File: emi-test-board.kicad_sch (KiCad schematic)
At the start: 1 part, among them U1 XL1509-3.3

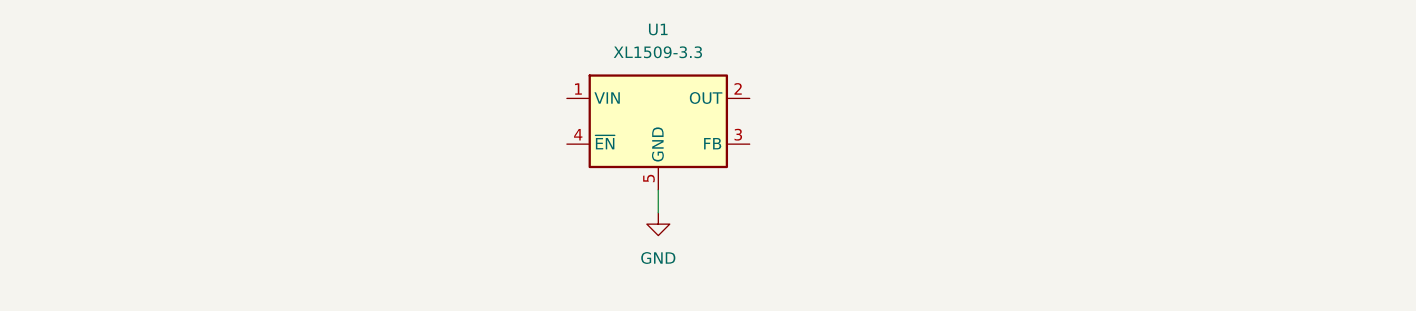
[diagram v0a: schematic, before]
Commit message: feat: XL1509-3.3 buck-converter schematic
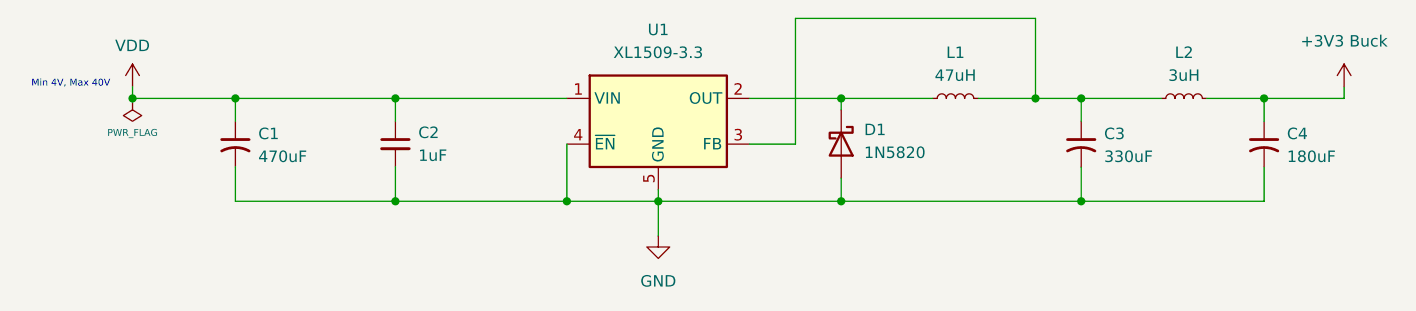
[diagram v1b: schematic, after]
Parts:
- added C1: 470uF, symbol Device:C_Small_US
- added C2: 1uF, symbol Device:C_Small
- added C3: 330uF, symbol Device:C_Small_US
- added C4: 180uF, symbol Device:C_Small_US
- added D1: 1N5820, symbol Device:D_Schottky
- added L1: 47uH, symbol Device:L_Small
- added L2: 3uH, symbol Device:L_Small
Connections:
- net GND: now also U1.4 (~{EN}), C1.2, C2.2, C3.2, C4.2, D1.2 (A)
- net VDD: now reaches U1.1 (VIN)
- net VDD: now also C1.1, C2.1
- net at U1.2 (OUT): now also D1.1 (K), L1.1
- net at U1.3 (FB): now also C3.1, L1.2, L2.1
- new net +3V3 Buck: C4.1, L2.2
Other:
- note added: "Min 4V, Max 40V"

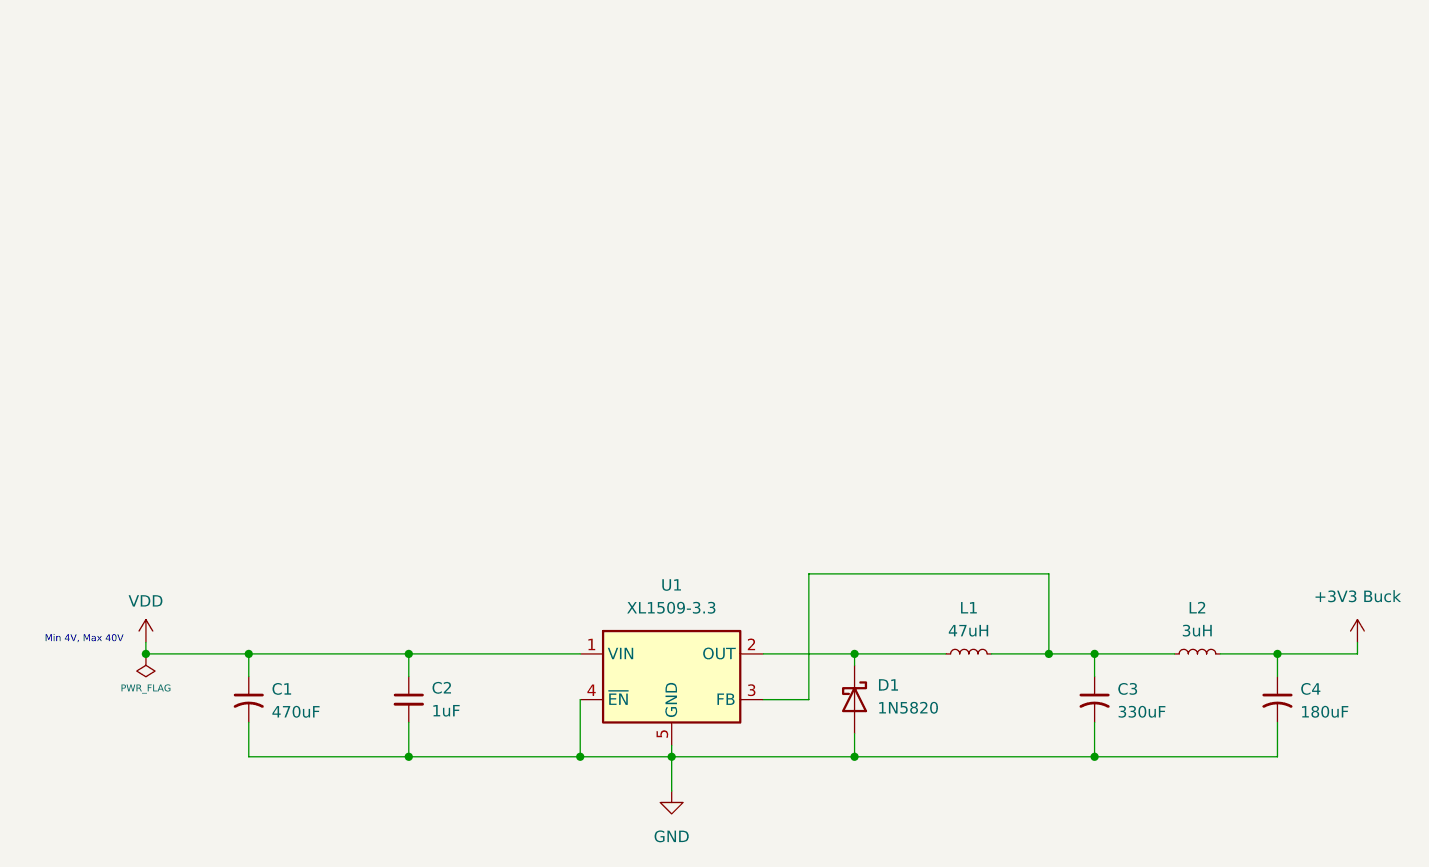
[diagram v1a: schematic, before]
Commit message: feat: component selection
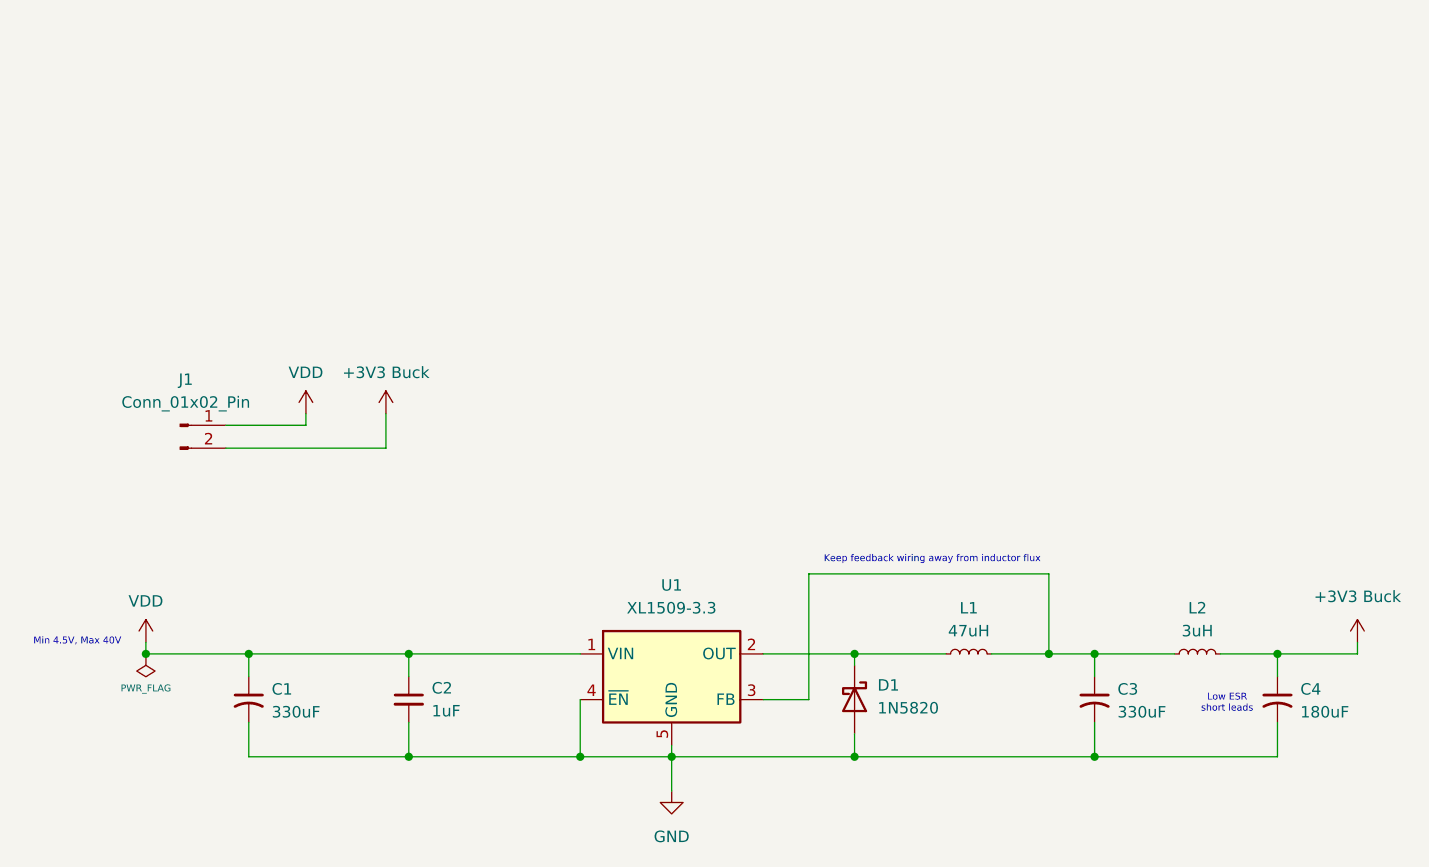
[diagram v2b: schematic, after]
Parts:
- added J1: Conn_01x02_Pin, Connector_PinHeader_2.54mm:PinHeader_1x02_P2.54mm_Horizontal, symbol Connector:Conn_01x02_Pin
- C1: value 470uF -> 330uF; footprint (none) -> project_footprints:PCAP_10x10-ELECT_NCA
- C2: footprint (none) -> Capacitor_SMD:C_0603_1608Metric_Pad1.08x0.95mm_HandSolder
- C3: footprint (none) -> project_footprints:PCAP_10x10-ELECT_NCA
- C4: footprint (none) -> Capacitor_THT:CP_Radial_D10.0mm_P5.00mm
- D1: footprint (none) -> Diode_THT:D_DO-201AD_P12.70mm_Horizontal
- L1: footprint (none) -> project_footprints:INDM3225X240N
- L2: footprint (none) -> project_footprints:IND_ASPI-0602S-3R0M-T
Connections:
- net +3V3 Buck: now also J1.2 (Pin_2)
- net VDD: now also J1.1 (Pin_1)
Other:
- note added: "Keep feedback wiring away from inductor flux"
- note added: "Low ESR short leads"
- note added: "Min 4.5V, Max 40V"
- note removed: "Min 4V, Max 40V"

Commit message: feat: layout and routing
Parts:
- C1, C3: footprint project_footprints:PCAP_10x10-ELECT_NCA -> Capacitor_THT:CP_Radial_D10.0mm_P5.00mm
- J1: footprint Connector_PinHeader_2.54mm:PinHeader_1x02_P2.54mm_Horizontal -> Connector_PinHeader_2.54mm:PinHeader_1x02_P2.54mm_Vertical
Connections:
- net BUCK_OUT: now reaches D1.1 (K), L1.1, U1.2 (OUT)
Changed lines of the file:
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@@
+		)
+	)
+	(label "BUCK_OUT"
+		(at 137.16 95.25 0)
+		(effects
+			(font
+				(size 0.762 0.762)
+			)
+			(justify left bottom)
 		)
 	)
@@
 			)
 		)
-		(property "Footprint" "Connector_PinHeader_2.54mm:PinHeader_1x02_P2.54mm_Horizontal"
+		(property "Footprint" "Connector_PinHeader_2.54mm:PinHeader_1x02_P2.54mm_Vertical"
 			(at 62.23 69.85 0)
 			(effects
@@
 			)
 		)
-		(property "Footprint" "project_footprints:PCAP_10x10-ELECT_NCA"
+		(property "Footprint" "Capacitor_THT:CP_Radial_D10.0mm_P5.00mm"
 			(at 163.83 100.33 0)
 			(effects
@@
 			)
 		)
-		(property "Description" "capacitor, small US symbol"
+		(property "Description" "C45107"
 			(at 163.83 100.33 0)
 			(effects
@@
 			)
 		)
-		(property "Footprint" "project_footprints:PCAP_10x10-ELECT_NCA"
+		(property "Footprint" "Capacitor_THT:CP_Radial_D10.0mm_P5.00mm"
 			(at 69.85 100.33 0)
 			(effects
@@
 			)
 		)
-		(property "Description" "capacitor, small US symbol"
+		(property "Description" "C45107"
 			(at 69.85 100.33 0)
 			(effects

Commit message: rework layout
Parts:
- removed C4: 180uF, Capacitor_THT:CP_Radial_D10.0mm_P5.00mm, symbol Device:C_Small_US
- removed L2: 3uH, project_footprints:IND_ASPI-0602S-3R0M-T, symbol Device:L_Small
- added J2: Conn_01x02_Pin, Connector_PinHeader_2.54mm:PinHeader_1x01_P2.54mm_Vertical, symbol Connector:Conn_01x01_Pin
- added J3: Barrel_Jack_Switch, symbol Connector:Barrel_Jack_Switch
- J1: footprint Connector_PinHeader_2.54mm:PinHeader_1x02_P2.54mm_Vertical -> Connector_PinHeader_2.54mm:PinHeader_1x01_P2.54mm_Vertical; symbol Connector:Conn_01x02_Pin -> Connector:Conn_01x01_Pin
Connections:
- net +3V3 Buck: now also C3.1, L1.2, U1.3 (FB), J2.1 (Pin_1); no longer J1.2 (Pin_2)
- net GND: now also J3.2, J3.3
- net BUCK_OUT renamed BUCK_SW
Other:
- note removed: "Low ESR short leads"

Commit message: finalize layout
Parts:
- J1: value Conn_01x02_Pin -> Conn_01x01_Pin
- J2: footprint Connector_PinHeader_2.54mm:PinHeader_1x01_P2.54mm_Vertical -> Connector_PinHeader_2.54mm:PinHeader_1x02_P2.54mm_Vertical; symbol Connector:Conn_01x01_Pin -> Connector:Conn_01x02_Pin
- J3: footprint (none) -> Connector_BarrelJack:BarrelJack_CUI_PJ-102AH_Horizontal; JLC (none) -> C3096093
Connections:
- net GND: now also J2.2 (Pin_2)
- net VDD: now also J3.1
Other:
- moved on the sheet: J1
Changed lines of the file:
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@@
+	)
+	(junction
+		(at 82.55 36.83)
+		(diameter 0)
+		(color 0 0 0 0)
 	)
 	(junction
@@
 	(wire
 		(pts
+			(xy 66.04 36.83) (xy 82.55 36.83)
+		)
+		(stroke
+			(width 0)
+			(type default)
+		)
+	)
+	(wire
+		(pts
 			(xy 137.16 104.14) (xy 137.16 106.68)
 		)
@@
 	(wire
 		(pts
+			(xy 72.39 46.99) (xy 82.55 46.99)
+		)
+		(stroke
+			(width 0)
+			(type default)
+		)
+	)
+	(wire
+		(pts
 			(xy 69.85 95.25) (xy 87.63 95.25)
 		)
@@
 	(wire
 		(pts
-			(xy 76.2 66.04) (xy 76.2 67.31)
-		)
-		(stroke
-			(width 0)
-			(type default)
-		)
-	)
-	(wire
-		(pts
 			(xy 87.63 102.87) (xy 87.63 106.68)
 		)
@@
 	(wire
 		(pts
+			(xy 72.39 80.01) (xy 72.39 81.28)
+		)
+		(stroke
+			(width 0)
+			(type default)
+		)
+	)
+	(wire
+		(pts
 			(xy 87.63 95.25) (xy 106.68 95.25)
 		)
@@
 	(wire
 		(pts
+			(xy 82.55 30.48) (xy 82.55 36.83)
+		)
+		(stroke
+			(width 0)
+			(type default)
+		)
+	)
+	(wire
+		(pts
+			(xy 82.55 36.83) (xy 82.55 46.99)
+		)
+		(stroke
+			(width 0)
+			(type default)
+		)
+	)
+	(wire
+		(pts
 			(xy 163.83 95.25) (xy 170.18 95.25)
 		)
@@
 	(wire
 		(pts
+			(xy 68.58 80.01) (xy 72.39 80.01)
+		)
+		(stroke
+			(width 0)
+			(type default)
+		)
+	)
+	(wire
+		(pts
 			(xy 69.85 106.68) (xy 69.85 102.87)
 		)
@@
 		(pts
 			(xy 72.39 49.53) (xy 72.39 52.07)
-		)
-		(stroke
-			(width 0)
-			(type default)
-		)
-	)
-	(wire
-		(pts
-			(xy 67.31 67.31) (xy 76.2 67.31)
 		)
 		(stroke
@@
 	(symbol
 		(lib_id "Connector:Conn_01x01_Pin")
-		(at 62.23 67.31 0)
+		(at 60.96 36.83 0)
 		(unit 1)
 		(exclude_from_sim no)
@@
 		(fields_autoplaced yes)
 		(property "Reference" "J1"
-			(at 62.865 62.23 0)
-			(effects
-				(font
-					(size 1.27 1.27)
-				)
-			)
-		)
-		(property "Value" "Conn_01x02_Pin"
-			(at 62.865 64.77 0)
+			(at 61.595 31.75 0)
+			(effects
+				(font
+					(size 1.27 1.27)
+				)
+			)
+		)
+		(property "Value" "Conn_01x01_Pin"
+			(at 61.595 34.29 0)
 			(effects
 				(font
@@
 		)
 		(property "Footprint" "Connector_PinHeader_2.54mm:PinHeader_1x01_P2.54mm_Vertical"
-			(at 62.23 67.31 0)
+			(at 60.96 36.83 0)
 			(effects
 				(font
@@
 		)
 		(property "Datasheet" "~"
-			(at 62.23 67.31 0)
+			(at 60.96 36.83 0)
 			(effects
 				(font
@@
 		)
 		(property "Description" "Generic connector, single row, 01x01, script generated"
-			(at 62.23 67.31 0)
+			(at 60.96 36.83 0)
 			(effects
 				(font
@@
 	)
 	(symbol
-		(lib_id "Connector:Conn_01x01_Pin")
+		(lib_id "Connector:Conn_01x02_Pin")
 		(at 63.5 77.47 0)
 		(unit 1)
@@
 			)
 		)
-		(property "Footprint" "Connector_PinHeader_2.54mm:PinHeader_1x01_P2.54mm_Vertical"
+		(property "Footprint" "Connector_PinHeader_2.54mm:PinHeader_1x02_P2.54mm_Vertical"
 			(at 63.5 77.47 0)
 			(effects
@@
 			)
 		)
-		(property "Description" "Generic connector, single row, 01x01, script generated"
+		(property "Description" "Generic connector, single row, 01x02, script generated"
 			(at 63.5 77.47 0)
 			(effects
@@
 		)
 		(pin "1"
+		)
+		(pin "2"
 		)
 		(instances
@@
 			)
 		)
-		(property "Footprint" ""
+		(property "Footprint" "Connector_BarrelJack:BarrelJack_CUI_PJ-102AH_Horizontal"
 			(at 66.04 50.546 0)
 			(effects
@@
 		)
 		(property "Description" "DC Barrel Jack with an internal switch"
+			(at 64.77 49.53 0)
+			(effects
+				(font
+					(size 1.27 1.27)
+				)
+				(hide yes)
+			)
+		)
+		(property "JLC" "C3096093"
 			(at 64.77 49.53 0)
 			(effects
@@
 	)
 	(symbol
+		(lib_id "power:GND")
+		(at 72.39 81.28 0)
+		(unit 1)
+		(exclude_from_sim no)
+		(in_bom yes)
+		(on_board yes)
+		(dnp no)
+		(fields_autoplaced yes)
+		(property "Reference" "#PWR07"
+			(at 72.39 87.63 0)
+			(effects
+				(font
+					(size 1.27 1.27)
+				)
+				(hide yes)
+			)
+		)
+		(property "Value" "GND"
+			(at 72.39 86.36 0)
+			(effects
+				(font
+					(size 1.27 1.27)
+				)
+			)
+		)
+		(property "Footprint" ""
+			(at 72.39 81.28 0)
+			(effects
+				(font
+					(size 1.27 1.27)
+				)
+				(hide yes)
+			)
+		)
+		(property "Datasheet" ""
+			(at 72.39 81.28 0)
+			(effects
+				(font
+					(size 1.27 1.27)
+				)
+				(hide yes)
+			)
+		)
+		(property "Description" "Power symbol creates a global label with name \"GND\" , ground"
+			(at 72.39 81.28 0)
+			(effects
+				(font
+					(size 1.27 1.27)
+				)
+				(hide yes)
+			)
+		)
+		(pin "1"
+		)
+		(instances
+			(project "emi-test-board"
+				(path "/79f480d4-ad37-4b66-a259-96ab4b59ec6d"
+					(reference "#PWR07")
+					(unit 1)
+				)
+			)
+		)
+	)
+	(symbol
 		(lib_id "Device:C_Small_US")
 		(at 69.85 100.33 0)
@@
 	)
 	(symbol
-		(lib_id "power:+3.3V")
-		(at 76.2 66.04 0)
-		(unit 1)
-		(exclude_from_sim no)
-		(in_bom yes)
-		(on_board yes)
-		(dnp no)
-		(property "Reference" "#PWR04"
-			(at 76.2 69.85 0)
-			(effects
-				(font
-					(size 1.27 1.27)
-				)
-				(hide yes)
-			)
-		)
-		(property "Value" "VDD"
-			(at 76.2 61.468 0)
-			(effects
-				(font
-					(size 1.27 1.27)
-				)
-			)
-		)
-		(property "Footprint" ""
-			(at 76.2 66.04 0)
-			(effects
-				(font
-					(size 1.27 1.27)
-				)
-				(hide yes)
-			)
-		)
-		(property "Datasheet" ""
-			(at 76.2 66.04 0)
-			(effects
-				(font
-					(size 1.27 1.27)
-				)
-				(hide yes)
-			)
-		)
-		(property "Description" "Power symbol creates a global label with name \"+3.3V\""
-			(at 76.2 66.04 0)
-			(effects
-				(font
-					(size 1.27 1.27)
-				)
-				(hide yes)
-			)
-		)
-		(pin "1"
-		)
-		(instances
-			(project "emi-test-board"
-				(path "/79f480d4-ad37-4b66-a259-96ab4b59ec6d"
-					(reference "#PWR04")
-					(unit 1)
-				)
-			)
-		)
-	)
-	(symbol
 		(lib_id "Device:C_Small")
 		(at 87.63 100.33 0)
@@
 					(unit 1)
 				)
+			)
+		)
+	)
+	(symbol
+		(lib_id "power:+3.3V")
+		(at 82.55 30.48 0)
+		(unit 1)
+		(exclude_from_sim no)
+		(in_bom yes)
+		(on_board yes)
+		(dnp no)
+		(property "Reference" "#PWR08"
+			(at 82.55 34.29 0)
+			(effects
+				(font
+					(size 1.27 1.27)
+				)
+				(hide yes)
+			)
+		)
+		(property "Value" "VDD"
+			(at 82.55 25.908 0)
+			(effects
+				(font
+					(size 1.27 1.27)
+				)
+			)
+		)
+		(property "Footprint" ""
+			(at 82.55 30.48 0)
+			(effects
+				(font
+					(size 1.27 1.27)
+				)
+				(hide yes)
+			)
+		)
+		(property "Datasheet" ""
+			(at 82.55 30.48 0)
+			(effects
+				(font
+					(size 1.27 1.27)
+				)
+				(hide yes)
+			)
+		)
+		(property "Description" "Power symbol creates a global label with name \"+3.3V\""
+			(at 82.55 30.48 0)
+			(effects
+				(font
+					(size 1.27 1.27)
+				)
+				(hide yes)
+			)
+		)
+		(pin "1"
+		)
+		(instances
+			(project "emi-test-board"
+				(path "/79f480d4-ad37-4b66-a259-96ab4b59ec6d"
+					(reference "#PWR08")
+					(unit 1)
+				)
